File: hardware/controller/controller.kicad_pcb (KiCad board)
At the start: 2 copper layers, 100 x 69 mm, 194 parts, among them J1 USB_C_Receptacle_USB2.0_14P, J10 Conn_01x01, J11 Conn_01x01, J12 Conn_02x03_Odd_Even, J2 IDC-10, J3 XT-60, J4 Conn_01x07, J5 Conn_01x01, J6 Conn_01x01, J7 Conn_01x01, J8 Conn_02x03_Odd_Even, J9 Conn_01x01, Q1 SUD50P04-08, Q10 AOD66406, Q11 AOD66406, Q12 AOD66406, Q13 AOD66406, Q2 AOD66406, Q3 AOD66406, Q4 AOD66406, Q5 AOD66406, Q6 AOD66406, Q7 AOD66406, Q8 AOD66406, Q9 AOD66406, SW1 SW_Push, SW2 SW_Push, SW3 SW_Push, SW4 JS102011SAQN, U1 SRV05-4, U10 LM2105D, U11 LMV331, U12 LM2105D, U13 LMV331, U14 LM2105D, U15 LMV331, U16 LM2105D, U17 LMV331, U18 LM2105D, U19 LMV331, U2 ESP32-C3-WROOM-02, U3 STM32U535RET6, U5 LM1117MP-3.3, U6 LV14340, U7 MPU-6050, U8 LM2105D, U9 LMV331, Y1 8MHz

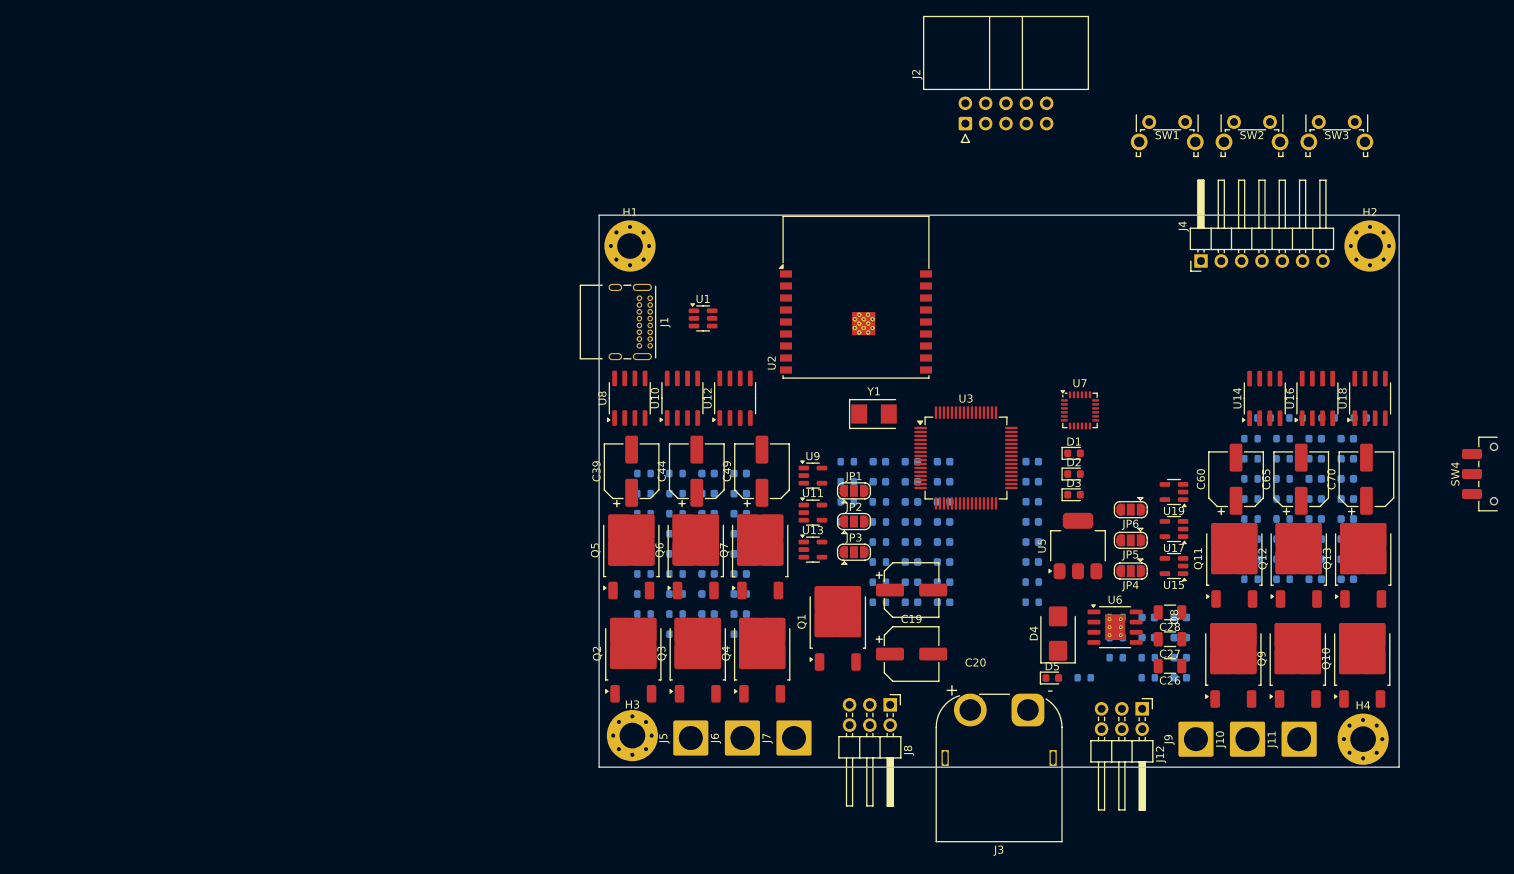
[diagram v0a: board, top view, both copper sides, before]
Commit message: add VBUS sense to STM and ESP, change buttons and sw to vertical, add USB-C to SEM
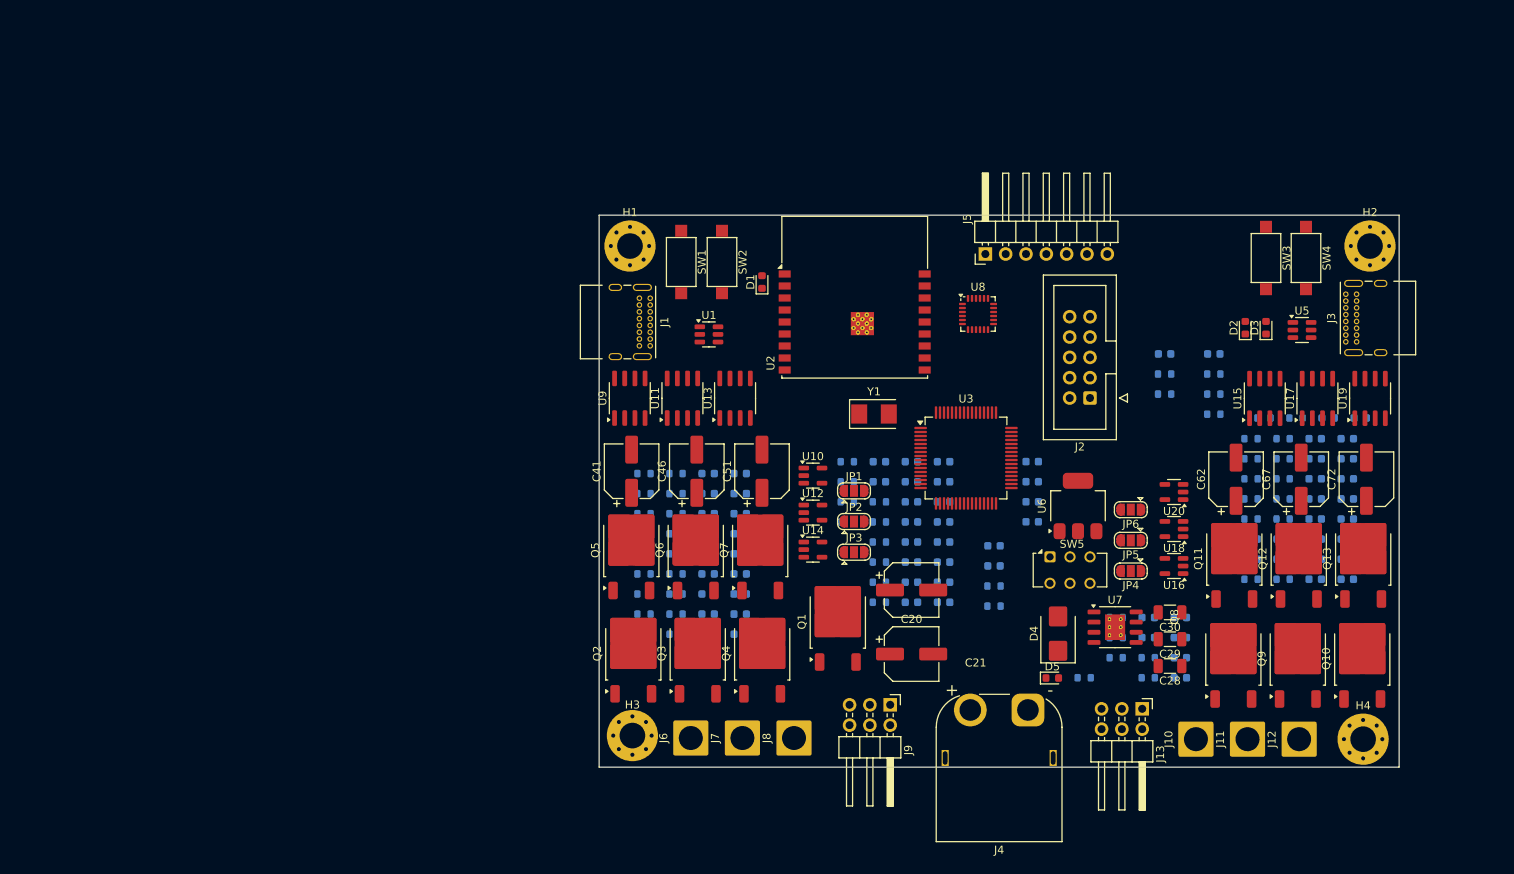
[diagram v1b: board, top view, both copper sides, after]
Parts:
- added C15: 100n, Capacitor_SMD:C_0603_1608Metric, B.Cu at (242.0, 67.0)
- added C22: 100n, Capacitor_SMD:C_0603_1608Metric, B.Cu at (235.8, 67.0)
- added J3: USB_C_Receptacle_USB2.0_14P, Connector_USB:USB_C_Receptacle_GCT_USB4085, F.Cu at (258.5, 65.5)
- added R12: 5.1k, Resistor_SMD:R_0603_1608Metric, B.Cu at (242.0, 72.0)
- added R13: 5.1k, Resistor_SMD:R_0603_1608Metric, B.Cu at (242.0, 74.5)
- added R15: 10k, Resistor_SMD:R_0603_1608Metric, B.Cu at (235.8, 69.5)
- added R17: 10k, Resistor_SMD:R_0603_1608Metric, B.Cu at (235.8, 72.0)
- added R9: 10k, Resistor_SMD:R_0603_1608Metric, B.Cu at (242.0, 69.5)
- added SW3: SW_Push, Button_Switch_SMD:SW_SPST_CK_RS282G05A3, F.Cu at (248.5, 55.0)
- added U5: SRV05-4, Package_TO_SOT_SMD:SOT-23-6, F.Cu at (253.0, 64.0)
- J2: footprint Connector_IDC:IDC-Header_2x05_P2.54mm_Horizontal -> Connector_IDC:IDC-Header_2x05_P2.54mm_Vertical
- SW1: renamed from SW2; footprint Button_Switch_THT:SW_Tactile_SPST_Angled_PTS645Vx58-2LFS -> Button_Switch_SMD:SW_SPST_CK_RS282G05A3
- SW2: renamed from SW1; footprint Button_Switch_THT:SW_Tactile_SPST_Angled_PTS645Vx58-2LFS -> Button_Switch_SMD:SW_SPST_CK_RS282G05A3
- SW4: renamed from SW3; footprint Button_Switch_THT:SW_Tactile_SPST_Angled_PTS645Vx58-2LFS -> Button_Switch_SMD:SW_SPST_CK_RS282G05A3
- SW5: renamed from SW4; value JS102011SAQN -> SW_SPST; footprint Button_Switch_SMD:SW_SPDT_CK_JS102011SAQN -> Button_Switch_THT:SW_CK_JS202011CQN_DPDT_Straight
- moved SW1 71.3 mm to (175.4, 55.5), turned to -90 degrees
- moved SW5 56.5 mm to (221.5, 92.4), turned to 0 degrees
- moved SW2 56.2 mm to (180.5, 55.5), turned to -90 degrees
- moved D1 44.5 mm to (185.5, 58.0), turned to 90 degrees
- moved J2 37.7 mm to (226.5, 72.5), turned to 180 degrees
- moved D3 31.8 mm to (248.5, 63.7), turned to 90 degrees
- moved D2 28.2 mm to (245.9, 63.7), turned to 90 degrees
- moved J5 27.0 mm to (213.4, 54.5)
- moved U8 17.5 mm to (212.5, 62.0)
- moved SW4 17.1 mm to (253.5, 55.0), turned to -90 degrees
- moved U6 5.00 mm to (225.0, 86.0)
- moved C36 4.80 mm to (214.5, 91.0)
- moved R23 4.80 mm to (214.5, 98.5)
- moved C37 4.80 mm to (214.5, 93.5)
- moved R22 4.80 mm to (214.5, 96.0)
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- renumbered C9 to C10, C15 to C16, C16 to C17, C17 to C18, C18 to C19, C19 to C20, C20 to C21, C21 to C23, C22 to C24, C23 to C25, C24 to C26, C25 to C27, C26 to C28, C27 to C29, C28 to C30, C29 to C31, C30 to C32, C31 to C33, C32 to C34, C33 to C35, C34 to C36, C35 to C37, C36 to C38, C37 to C39, C38 to C40, C39 to C41, C40 to C42, C41 to C43, C42 to C44, C43 to C45, C44 to C46, C45 to C47, C46 to C48, C47 to C49, C7 to C5, C48 to C50, C49 to C51, C50 to C52, C51 to C53, C52 to C54, C53 to C55, C54 to C56, C55 to C57, C56 to C58, C57 to C59, C8 to C6, C58 to C60, C59 to C61, C60 to C62, C61 to C63, C62 to C64, C63 to C65, C64 to C66, C65 to C67, C66 to C68, C67 to C69, C5 to C7, C68 to C70, C69 to C71, C70 to C72, C71 to C73, C72 to C74, C73 to C75, C74 to C76, C75 to C77, C76 to C78, C77 to C79, C6 to C8, C10 to C9, J9 to J10, J10 to J11, J11 to J12, J12 to J13, J3 to J4, J4 to J5, J5 to J6, J6 to J7, J7 to J8, J8 to J9, R2 to R1, R9 to R10, R10 to R11, R11 to R14, R12 to R16, R13 to R18, R14 to R19, R1 to R2, R15 to R20, R16 to R21, R17 to R22, R18 to R23, R19 to R24, R20 to R25, R21 to R26, R22 to R27, R23 to R28, R24 to R29, R25 to R30, R26 to R31, R27 to R32, R28 to R33, R29 to R34, R30 to R35, R31 to R36, R32 to R37, R33 to R38, R34 to R39, R35 to R40, R36 to R41, R37 to R42, R38 to R43, R39 to R44, R40 to R45, R41 to R46, R42 to R47, R43 to R48, R44 to R49, R45 to R50, R46 to R51, R47 to R52, R48 to R53, R49 to R54, R50 to R55, R51 to R56, R52 to R57, R53 to R58, R54 to R59, U9 to U10, U10 to U11, U11 to U12, U12 to U13, U13 to U14, U14 to U15, U15 to U16, U16 to U17, U17 to U18, U18 to U19, U19 to U20, U5 to U6, U6 to U7, U7 to U8, U8 to U9
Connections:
- net /microcontroller/ESP_CC1 renamed /microcontroller/ESP_USB_CC1
- net /microcontroller/ESP_CC2 renamed /microcontroller/ESP_USB_CC2
- net /microcontroller/ESP_D+ renamed /microcontroller/ESP_USB_D+
- net /microcontroller/ESP_D- renamed /microcontroller/ESP_USB_D-
- net /microcontroller/ESP_VBUS renamed /microcontroller/ESP_USB_VBUS
- net /microcontroller/OSC_IN renamed /microcontroller/STM_OSC_IN
- net /microcontroller/OSC_OUT renamed /microcontroller/STM_OSC_OUT
- net /microcontroller/RESET renamed /microcontroller/STM_RESET
- net /microcontroller/SWCLK renamed /microcontroller/STM_SWCLK
- net /microcontroller/SWDIO renamed /microcontroller/STM_SWDIO
- net /microcontroller/SWO renamed /microcontroller/STM_SWO
- net /microcontroller/VCAP renamed /microcontroller/STM_VCAP
- R16 pad 2: Net-(SW4-B) -> Net-(SW5-A)
- SW5 pad 1: GND -> Net-(SW5-A)
- SW5 pad 2: Net-(SW4-B) -> GND
- SW5 pad 3: unconnected-(SW4-C-Pad3) -> (no net)
- U2 pad 15: unconnected-(U2-IO3-Pad15) -> VBUS_SENSE
- U3 pad 24: unconnected-(U3-PC4-Pad24) -> VBUS_SENSE
- U3 pad 44: unconnected-(U3-PA11-Pad44) -> /microcontroller/STM_USB_D-
- U3 pad 45: unconnected-(U3-PA12-Pad45) -> /microcontroller/STM_USB_D+
- U3 pad 60: GND -> /microcontroller/STM_BOOT0

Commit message: USBLC6, IR2101
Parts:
- added D10: 1N5819HW-7-F, Diode_SMD:Nexperia_CFP3_SOD-123W, F.Cu at (235.8, 77.6)
- added D11: 1N5819HW-7-F, Diode_SMD:Nexperia_CFP3_SOD-123W, F.Cu at (239.0, 77.6)
- added D6: 1N5819HW-7-F, Diode_SMD:Nexperia_CFP3_SOD-123W, F.Cu at (187.0, 74.0)
- added D7: 1N5819HW-7-F, Diode_SMD:Nexperia_CFP3_SOD-123W, F.Cu at (190.2, 74.0)
- added D8: 1N5819HW-7-F, Diode_SMD:Nexperia_CFP3_SOD-123W, F.Cu at (193.5, 74.0)
- added D9: 1N5819HW-7-F, Diode_SMD:Nexperia_CFP3_SOD-123W, F.Cu at (232.5, 77.6)
- C11: value 100n -> 10u
- C12: value 1u -> 100n
- C39, C44, C49, C60, C65, C70: value 100n/50V -> 1u/50V
- C8: value 10u -> 100n
- C9: value 100n -> 1u
- R1, R2: value 10k -> 5.1k
- R15: value 10k -> 51k
- R24, R28, R30, R35, R37, R41, R42, R46, R48, R53, R55, R59: value 20 -> 100
- R5, R6: value 5.1k -> 10k
- R7: value 10k -> 1k
- R8: value 1k -> 10k
- U1, U5: value SRV05-4 -> USBLC6-2SC6
- U11, U13, U15, U17, U19, U9: value LM2105D -> IR2101
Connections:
- C7 pad 1: +3.3V -> /microcontroller/STM_RESET
- C9 pad 1: /microcontroller/STM_RESET -> +3.3V
- J1 pad A6: /microcontroller/ESP_USB_D+ -> Net-(J1-D+-PadA6)
- J1 pad A7: /microcontroller/ESP_USB_D- -> Net-(J1-D--PadA7)
- J1 pad B6: /microcontroller/ESP_USB_D+ -> Net-(J1-D+-PadA6)
- J1 pad B7: /microcontroller/ESP_USB_D- -> Net-(J1-D--PadA7)
- J3 pad A6: /microcontroller/STM_USB_D+ -> Net-(J3-D+-PadA6)
- J3 pad A7: /microcontroller/STM_USB_D- -> Net-(J3-D--PadA7)
- J3 pad B6: /microcontroller/STM_USB_D+ -> Net-(J3-D+-PadA6)
- J3 pad B7: /microcontroller/STM_USB_D- -> Net-(J3-D--PadA7)
- R1 pad 1: +3.3V -> GND
- R1 pad 2: /microcontroller/STM_RESET -> /microcontroller/ESP_USB_CC1
- R2 pad 1: +3.3V -> /microcontroller/ESP_USB_CC2
- R2 pad 2: /microcontroller/ESP_EN -> GND
- R3 pad 2: /microcontroller/ESP_IO8 -> /microcontroller/STM_RESET
- R4 pad 2: /microcontroller/ESP_IO2 -> /microcontroller/ESP_EN
- R5 pad 1: GND -> +3.3V
- R5 pad 2: /microcontroller/ESP_USB_CC1 -> /microcontroller/ESP_IO8
- R6 pad 1: /microcontroller/ESP_USB_CC2 -> +3.3V
- R6 pad 2: GND -> /microcontroller/ESP_IO2
- R7 pad 1: +3.3V -> /microcontroller/ESP_LED
- R7 pad 2: /microcontroller/ESP_BOOT -> Net-(D1-A)
- R8 pad 1: /microcontroller/ESP_LED -> +3.3V
- R8 pad 2: Net-(D1-A) -> /microcontroller/ESP_BOOT
- U1 pad 4: unconnected-(U1-IO3-Pad4) -> Net-(J1-D+-PadA6)
- U1 pad 6: unconnected-(U1-IO4-Pad6) -> Net-(J1-D--PadA7)
- U5 pad 4: unconnected-(U5-IO3-Pad4) -> Net-(J3-D+-PadA6)
- U5 pad 6: unconnected-(U5-IO4-Pad6) -> Net-(J3-D--PadA7)

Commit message: custom footprints with all 3D models
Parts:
- removed C78: 10u, Capacitor_SMD:C_0603_1608Metric
- removed C79: 100n, Capacitor_SMD:C_0603_1608Metric
- added L1: 6.8u/4.5A, hogger2:PA4341.XXXNLT, F.Cu at (150.4, 103.0)
- added U4: nRF24L01+ 2.4Gz Mini SMD, hogger2:nRF24L01p_Mini_SMD, B.Cu at (174.4, 68.5)
- C20, C51, C72: value 47u/50V -> 100n; footprint Capacitor_SMD:CP_Elec_6.3x7.7 -> Capacitor_SMD:C_0603_1608Metric; moved to B.Cu
- C21: value 47u/50V -> 100n/16V; footprint Capacitor_SMD:CP_Elec_6.3x7.7 -> Capacitor_SMD:C_0603_1608Metric; moved to B.Cu
- C23: value 100n/16V -> 4.7u
- C24: value 100n -> 4.7u
- C25: value 4.7u -> 100n
- C26: value 4.7u -> 10u/50V; footprint Capacitor_SMD:C_0603_1608Metric -> Capacitor_SMD:C_1206_3216Metric; moved to F.Cu
- C27: value 100n -> 47u/16V; footprint Capacitor_SMD:C_0603_1608Metric -> Capacitor_SMD:C_1206_3216Metric; moved to F.Cu
- C28: value 10u/50V -> 47u/16V
- C29: value 47u/16V -> 22n; footprint Capacitor_SMD:C_1206_3216Metric -> Capacitor_SMD:C_0603_1608Metric
- C30: value 47u/16V -> 100n; footprint Capacitor_SMD:C_1206_3216Metric -> Capacitor_SMD:C_0603_1608Metric
- C31: value 22n -> 100n
- C32, C53, C74: value 100n -> 10u
- C34, C56, C77: value 10u -> 100n
- C35: value 100n -> 2n2
- C36, C58: value 100n -> 1u/50V
- C37: value 2n2 -> 1u/50V
- C38, C43, C48, C59, C64, C69: value 1u/50V -> 100n
- C39, C44, C49, C60, C65, C70: value 1u/50V -> 47u/50V; footprint Capacitor_SMD:C_0603_1608Metric -> Capacitor_SMD:CP_Elec_6.3x7.7; moved to F.Cu
- C40, C45, C50, C61, C66, C71: value 100n -> 1n
- C41, C46, C62, C67: value 47u/50V -> 1u/50V; footprint Capacitor_SMD:CP_Elec_6.3x7.7 -> Capacitor_SMD:C_0603_1608Metric; moved to B.Cu
- C42, C47, C63, C68: value 1n -> 1u/50V
- C52, C73: value 1n -> 10u
- C57: value 10u -> 1u/50V
- J4: footprint Connector_AMASS:AMASS_XT60PW-M_1x02_P7.20mm_Horizontal -> hogger2:XT60PW-M
- SW1, SW2, SW3, SW4: footprint Button_Switch_SMD:SW_SPST_CK_RS282G05A3 -> hogger2:spst_6x3mm
- U7: footprint Package_SO:SOIC-8-1EP_3.9x4.9mm_P1.27mm_EP2.514x3.2mm_ThermalVias -> hogger2:LV14340
- U8: footprint Sensor_Motion:InvenSense_QFN-24_4x4mm_P0.5mm -> hogger2:MPU6050_handsolder
- moved J3 152.5 mm to (106.0, 61.0), turned to -90 degrees
- moved U5 141.1 mm to (111.9, 64.4), turned to 180 degrees
- moved SW4 138.1 mm to (115.4, 56.5)
- moved SW3 138.0 mm to (110.5, 56.5)
- moved D3 132.7 mm to (115.9, 66.9), turned to 180 degrees
- moved D2 130.2 mm to (115.9, 68.9), turned to 180 degrees
- moved J2 96.1 mm to (130.5, 66.5)
- moved C26 94.9 mm to (143.0, 103.0), turned to 0 degrees
- moved C27 91.1 mm to (143.0, 107.0), turned to 0 degrees
- moved D5 85.8 mm to (138.0, 89.0)
- moved U6 85.5 mm to (140.0, 95.0), turned to 180 degrees
- moved C60 79.5 mm to (179.4, 83.4), turned to -90 degrees
- moved R18 78.0 mm to (151.9, 103.3)
- moved R19 78.0 mm to (151.9, 105.8)
- moved R20 78.0 mm to (151.9, 108.4)
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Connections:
- C20 pad 1: /power/BATTERY_IN -> VBUS_SENSE
- C21 pad 1: VBUS -> Net-(U7-BOOT)
- C21 pad 2: GND -> Net-(D4-K)
- C22 pad 1: VBUS_SENSE -> +5V
- C23 pad 1: Net-(U7-BOOT) -> +5V
- C23 pad 2: Net-(D4-K) -> GND
- C24 pad 1: +5V -> +3.3V
- C25 pad 1: +5V -> +3.3V
- C26 pad 1: +3.3V -> VBUS
- C27 pad 1: +3.3V -> +5V
- C28 pad 1: VBUS -> +5V
- C29 pad 1: +5V -> Net-(U7-SS)
- C30 pad 1: +5V -> +3.3V
- C31 pad 1: Net-(U7-SS) -> +3.3V
- C34 pad 1: +3.3V -> /sensors/IMU_REGOUT
- C35 pad 1: +3.3V -> /sensors/IMU_CPOUT
- C36 pad 1: /sensors/IMU_REGOUT -> GND
- C36 pad 2: GND -> VBUS
- C37 pad 1: /sensors/IMU_CPOUT -> Net-(D6-K)
- C37 pad 2: GND -> /hog1/PHASE_U
- C38 pad 2: VBUS -> +3.3V
- C39 pad 1: Net-(D6-K) -> VBUS
- C39 pad 2: /hog1/PHASE_U -> GND
- C40 pad 1: GND -> /hog1/BEMF_U
- C40 pad 2: +3.3V -> GND
- C41 pad 1: VBUS -> GND
- C41 pad 2: GND -> VBUS
- C42 pad 1: /hog1/BEMF_U -> Net-(D7-K)
- C42 pad 2: GND -> /hog1/PHASE_V
- C43 pad 2: VBUS -> +3.3V
- C44 pad 1: Net-(D7-K) -> VBUS
- C44 pad 2: /hog1/PHASE_V -> GND
- C45 pad 1: GND -> /hog1/BEMF_V
- C45 pad 2: +3.3V -> GND
- C46 pad 1: VBUS -> GND
- C46 pad 2: GND -> VBUS
- C47 pad 1: /hog1/BEMF_V -> Net-(D8-K)
- C47 pad 2: GND -> /hog1/PHASE_W
- C48 pad 2: VBUS -> +3.3V
- C49 pad 1: Net-(D8-K) -> VBUS
- C49 pad 2: /hog1/PHASE_W -> GND
- C50 pad 1: GND -> /hog1/BEMF_W
- C50 pad 2: +3.3V -> GND
- C51 pad 1: VBUS -> +5V
- C52 pad 1: /hog1/BEMF_W -> +5V
- C57 pad 1: +5V -> GND
- C57 pad 2: GND -> VBUS
- C58 pad 1: +5V -> Net-(D9-K)
- C58 pad 2: GND -> /hog2/PHASE_U
- C59 pad 2: VBUS -> +3.3V
- C60 pad 1: Net-(D9-K) -> VBUS
- C60 pad 2: /hog2/PHASE_U -> GND
- C61 pad 1: GND -> /hog2/BEMF_U
- C61 pad 2: +3.3V -> GND
- C62 pad 1: VBUS -> GND
- C62 pad 2: GND -> VBUS
- C63 pad 1: /hog2/BEMF_U -> Net-(D10-K)
- C63 pad 2: GND -> /hog2/PHASE_V
- C64 pad 2: VBUS -> +3.3V
- C65 pad 1: Net-(D10-K) -> VBUS
- C65 pad 2: /hog2/PHASE_V -> GND
- C66 pad 1: GND -> /hog2/BEMF_V
- C66 pad 2: +3.3V -> GND
- C67 pad 1: VBUS -> GND
- C67 pad 2: GND -> VBUS
- C68 pad 1: /hog2/BEMF_V -> Net-(D11-K)
- C68 pad 2: GND -> /hog2/PHASE_W
- C69 pad 2: VBUS -> +3.3V
- C70 pad 1: Net-(D11-K) -> VBUS
- C70 pad 2: /hog2/PHASE_W -> GND
- C71 pad 1: GND -> /hog2/BEMF_W
- C71 pad 2: +3.3V -> GND
- C72 pad 1: VBUS -> +5V
- C73 pad 1: /hog2/BEMF_W -> +5V
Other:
- board size 100 x 69 mm -> 100 x 70 mm
